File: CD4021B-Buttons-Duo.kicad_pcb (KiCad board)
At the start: 2 copper layers, 99.1 x 50.8 mm, 49 parts, among them J1 2.54, J10 JST XH, J11 JST XH, J12 JST XH, J13 JST XH, J14 JST XH, J15 JST XH, J16 JST XH, J17 JST XH, J2 JST XH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

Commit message: Cleanup via stitches
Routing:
- net GND: track 119.8 -> 111.2 mm, vias 49 -> 40
- net VCC: track 88.0 -> 93.0 mm
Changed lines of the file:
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@@
 (kicad_pcb (version 4) (host pcbnew 4.0.7)
   (general
-    (links 0)
-    (no_connects 2)
-    (area 105.334999 78.918999 204.545001 129.869001)
+    (links 153)
+    (no_connects 0)
+    (area 97.409048 78.918999 212.470953 129.869001)
     (thickness 1.6)
     (drawings 23)
-    (tracks 451)
+    (tracks 431)
     (zones 0)
     (modules 49)
@@
   (gr_line (start 204.47 78.994) (end 204.47 129.794) (layer Edge.Cuts) (width 0.15))
   (gr_line (start 105.41 78.994) (end 204.47 78.994) (layer Edge.Cuts) (width 0.15))
+  (segment (start 173.736 101.854) (end 175.26 101.854) (width 0.5) (layer F.Cu) (net 1) (status 30))
+  (segment (start 131.760454 101.838502) (end 133.284454 101.838502) (width 0.5) (layer F.Cu) (net 1) (status 30))
+  (segment (start 144.272 107.188) (end 142.24 107.188) (width 0.5) (layer B.Cu) (net 1) (status 30))
+  (segment (start 161.29 113.538) (end 161.29 122.428) (width 1) (layer B.Cu) (net 1))
+  (segment (start 154.94 107.188) (end 161.29 113.538) (width 1) (layer B.Cu) (net 1))
+  (segment (start 144.272 107.188) (end 154.94 107.188) (width 1) (layer B.Cu) (net 1) (status 10))
+  (via (at 161.29 122.428) (size 1.5) (drill 1.2) (layers F.Cu B.Cu) (net 1))
+  (segment (start 161.29 93.726) (end 161.29 86.614) (width 1) (layer F.Cu) (net 1))
   (segment (start 136.792 121.688) (end 139.192 121.688) (width 0.25) (layer F.Cu) (net 1) (status 30))
   (segment (start 136.792 86.36) (end 139.192 86.36) (width 0.25) (layer F.Cu) (net 1) (status 30))
   (segment (start 177.432 121.666) (end 179.832 121.666) (width 0.25) (layer F.Cu) (net 1) (status 30))
   (segment (start 177.432 86.338) (end 179.832 86.338) (width 0.25) (layer F.Cu) (net 1) (status 30))
-  (segment (start 144.272 107.188) (end 144.526 106.934) (width 1) (layer B.Cu) (net 1) (status 30))
-  (segment (start 144.526 106.934) (end 154.686 106.934) (width 1) (layer B.Cu) (net 1) (status 10))
-  (segment (start 154.686 106.934) (end 161.29 113.538) (width 1) (layer B.Cu) (net 1))
-  (segment (start 161.29 113.538) (end 161.29 119.126) (width 1) (layer B.Cu) (net 1))
-  (via (at 161.29 119.126) (size 1.5) (drill 1.2) (layers F.Cu B.Cu) (net 1))
   (segment (start 139.192008 105.917992) (end 139.192 105.918) (width 0.25) (layer F.Cu) (net 1))
   (segment (start 142.24 105.917992) (end 139.192008 105.917992) (width 0.25) (layer F.Cu) (net 1))
@@
   (segment (start 142.24 107.188) (end 142.24 105.917992) (width 0.25) (layer B.Cu) (net 1) (status 10))
   (via (at 142.24 105.917992) (size 0.6) (drill 0.4) (layers F.Cu B.Cu) (net 1))
-  (segment (start 142.24 107.188) (end 144.272 107.188) (width 1) (layer B.Cu) (net 1) (status 30))
   (segment (start 130.369956 101.854) (end 114.554 101.854) (width 1) (layer F.Cu) (net 1))
   (segment (start 173.736 101.854) (end 169.418 101.854) (width 1) (layer F.Cu) (net 1) (status 10))
   (segment (start 169.418 101.854) (end 161.29 93.726) (width 1) (layer F.Cu) (net 1))
-  (segment (start 161.29 93.726) (end 161.29 88.392) (width 1) (layer F.Cu) (net 1))
-  (segment (start 131.760454 101.838502) (end 133.104443 101.838502) (width 1) (layer F.Cu) (net 1) (status 30))
-  (segment (start 173.736 101.854) (end 175.26 101.854) (width 1) (layer F.Cu) (net 1) (status 30))
   (segment (start 131.760454 101.838502) (end 130.385454 101.838502) (width 1) (layer F.Cu) (net 1) (status 10))
   (segment (start 130.385454 101.838502) (end 130.369956 101.854) (width 1) (layer F.Cu) (net 1))
@@
   (via (at 167.64 102.616) (size 0.6) (drill 0.4) (layers F.Cu B.Cu) (net 2))
   (segment (start 152.654 105.156) (end 151.638 105.156) (width 0.25) (layer F.Cu) (net 2))
-  (via (at 151.638 105.156) (size 0.6) (drill 0.4) (layers F.Cu B.Cu) (net 2))
-  (segment (start 153.67 105.156) (end 152.654 105.156) (width 0.25) (layer B.Cu) (net 2))
-  (via (at 152.654 105.156) (size 0.6) (drill 0.4) (layers F.Cu B.Cu) (net 2))
-  (segment (start 154.686 105.156) (end 153.67 105.156) (width 0.25) (layer F.Cu) (net 2))
-  (via (at 153.67 105.156) (size 0.6) (drill 0.4) (layers F.Cu B.Cu) (net 2))
-  (segment (start 155.702006 105.156) (end 154.686 105.156) (width 0.25) (layer B.Cu) (net 2))
-  (via (at 154.686 105.156) (size 0.6) (drill 0.4) (layers F.Cu B.Cu) (net 2))
-  (segment (start 155.570006 105.288) (end 155.702006 105.156) (width 0.25) (layer B.Cu) (net 2))
-  (segment (start 155.702006 105.156006) (end 155.702006 105.156) (width 0.25) (layer B.Cu) (net 2))
-  (segment (start 156.464 105.918) (end 155.702006 105.156006) (width 0.25) (layer B.Cu) (net 2))
-  (via (at 155.702006 105.156) (size 0.6) (drill 0.4) (layers F.Cu B.Cu) (net 2))
-  (segment (start 157.226 106.68) (end 156.464 105.918) (width 0.25) (layer B.Cu) (net 2))
-  (via (at 156.464 105.918) (size 0.6) (drill 0.4) (layers F.Cu B.Cu) (net 2))
-  (segment (start 158.75 108.204) (end 159.512 108.966) (width 0.25) (layer F.Cu) (net 2))
-  (via (at 159.512 108.966) (size 0.6) (drill 0.4) (layers F.Cu B.Cu) (net 2))
-  (segment (start 157.988 107.442) (end 158.75 108.204) (width 0.25) (layer B.Cu) (net 2))
-  (via (at 158.75 108.204) (size 0.6) (drill 0.4) (layers F.Cu B.Cu) (net 2))
-  (segment (start 157.226 106.68) (end 157.988 107.442) (width 0.25) (layer F.Cu) (net 2))
-  (via (at 157.988 107.442) (size 0.6) (drill 0.4) (layers F.Cu B.Cu) (net 2))
-  (via (at 157.226 106.68) (size 0.6) (drill 0.4) (layers F.Cu B.Cu) (net 2))
+  (via (at 151.638 105.156) (size 0.6) (drill 0.4) (layers F.Cu B.Cu) (net 2) (status 1000000))
   (segment (start 110.236 109.474) (end 118.364 109.474) (width 1) (layer B.Cu) (net 2) (status 10))
   (segment (start 153.096 122.682) (end 154.94 122.682) (width 0.5) (layer B.Cu) (net 3) (status 30))

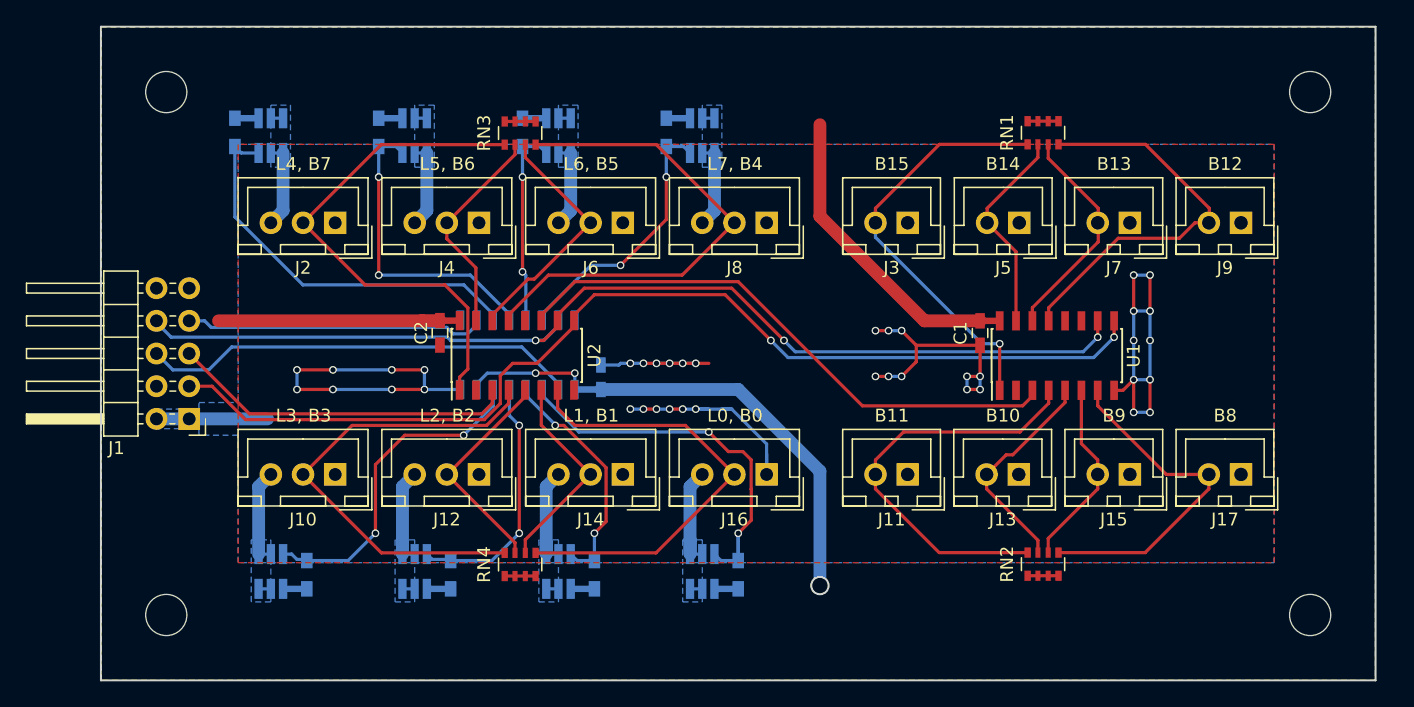
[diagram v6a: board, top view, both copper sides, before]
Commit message: Change the board dimension to be exactly 100x50mm
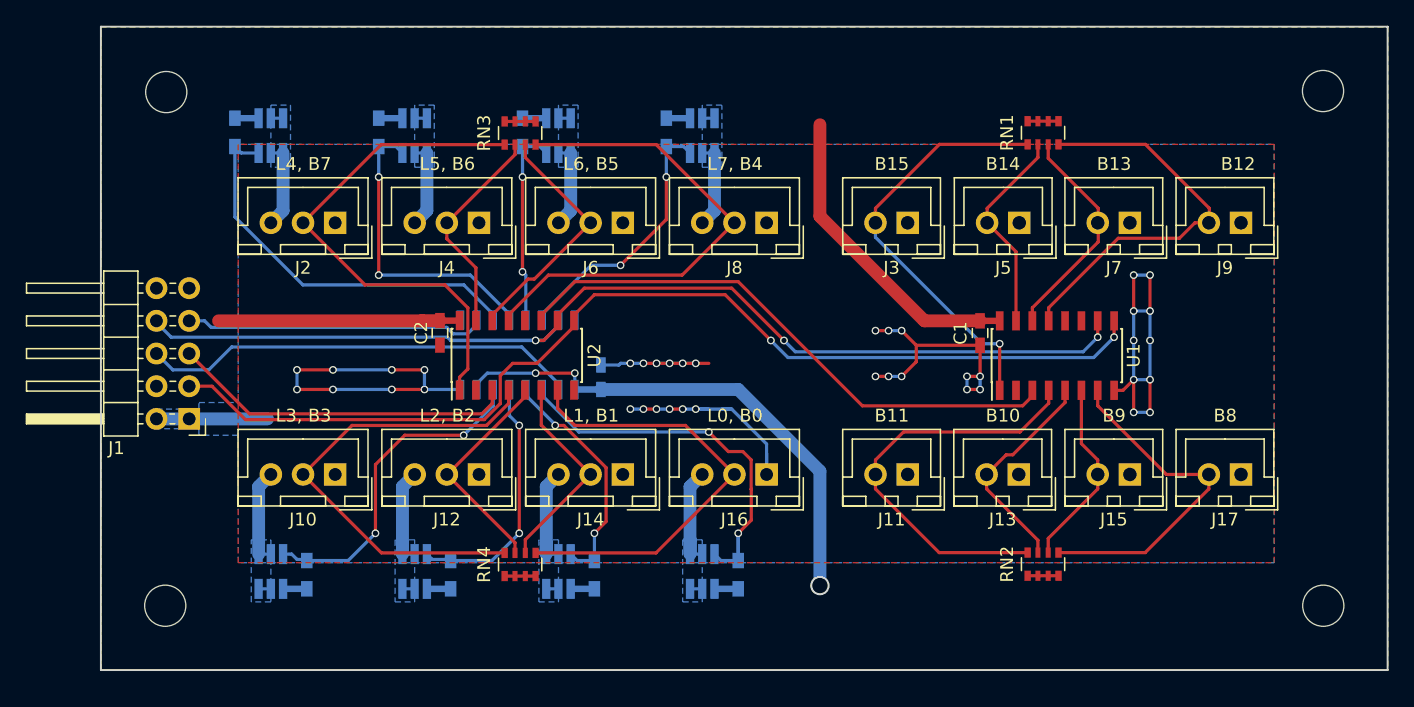
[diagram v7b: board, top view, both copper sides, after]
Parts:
- moved REF** 1.25 mm to (200.4, 124.0)
- moved REF** 1.00 mm to (200.4, 84.0)
- moved REF** 0.72 mm to (110.4, 124.0)
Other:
- board size 99.1 x 50.8 mm -> 100 x 50 mm
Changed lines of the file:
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@@
     (links 153)
     (no_connects 0)
-    (area 97.409048 78.918999 212.470953 129.869001)
+    (area 105.334999 78.918999 205.485001 129.069001)
     (thickness 1.6)
     (drawings 23)
@@
     (pad_to_mask_clearance 0)
     (aux_axis_origin 0 0)
+    (grid_origin 105.41 78.994)
     (visible_elements FFFFFF7F)
     (pcbplotparams
@@
   )
   (module Mounting_Holes:MountingHole_3.2mm_M3_ISO7380 (layer F.Cu)
-    (at 199.39 124.714)
+    (at 200.41 123.994)
     (descr "Mounting Hole 3.2mm, no annular, M3, ISO7380")
     (tags "mounting hole 3.2mm no annular m3 iso7380")
@@
   )
   (module Mounting_Holes:MountingHole_3.2mm_M3_ISO7380 (layer F.Cu)
-    (at 110.49 124.714)
+    (at 110.41 123.994)
     (descr "Mounting Hole 3.2mm, no annular, M3, ISO7380")
     (tags "mounting hole 3.2mm no annular m3 iso7380")
@@
   )
   (module Mounting_Holes:MountingHole_3.2mm_M3_ISO7380 (layer F.Cu)
-    (at 199.39 84.074)
+    (at 200.39 83.994)
     (descr "Mounting Hole 3.2mm, no annular, M3, ISO7380")
     (tags "mounting hole 3.2mm no annular m3 iso7380")
@@
     (effects (font (size 1 1) (thickness 0.15)))
   )
-  (gr_text B12 (at 192.786 89.662) (layer F.SilkS)
+  (gr_text B12 (at 193.786 89.662) (layer F.SilkS)
     (effects (font (size 1 1) (thickness 0.15)))
   )
@@
     (effects (font (size 1.5 1.5) (thickness 0.3)) (justify left mirror))
   )
-  (gr_line (start 105.41 129.794) (end 105.41 78.994) (layer Edge.Cuts) (width 0.15))
-  (gr_line (start 204.47 129.794) (end 105.41 129.794) (layer Edge.Cuts) (width 0.15))
-  (gr_line (start 204.47 78.994) (end 204.47 129.794) (layer Edge.Cuts) (width 0.15))
-  (gr_line (start 105.41 78.994) (end 204.47 78.994) (layer Edge.Cuts) (width 0.15))
+  (gr_line (start 105.41 128.994) (end 105.41 78.994) (layer Edge.Cuts) (width 0.15))
+  (gr_line (start 205.41 128.994) (end 105.41 128.994) (layer Edge.Cuts) (width 0.15))
+  (gr_line (start 205.41 78.994) (end 205.41 128.994) (layer Edge.Cuts) (width 0.15))
+  (gr_line (start 105.41 78.994) (end 205.41 78.994) (layer Edge.Cuts) (width 0.15))
   (segment (start 173.736 101.854) (end 175.26 101.854) (width 0.5) (layer F.Cu) (net 1) (status 30))
   (segment (start 131.760454 101.838502) (end 133.284454 101.838502) (width 0.5) (layer F.Cu) (net 1) (status 30))
@@
   (via (at 167.64 102.616) (size 0.6) (drill 0.4) (layers F.Cu B.Cu) (net 2))
   (segment (start 152.654 105.156) (end 151.638 105.156) (width 0.25) (layer F.Cu) (net 2))
-  (via (at 151.638 105.156) (size 0.6) (drill 0.4) (layers F.Cu B.Cu) (net 2) (status 1000000))
+  (via (at 151.638 105.156) (size 0.6) (drill 0.4) (layers F.Cu B.Cu) (net 2))
   (segment (start 110.236 109.474) (end 118.364 109.474) (width 1) (layer B.Cu) (net 2) (status 10))
   (segment (start 153.096 122.682) (end 154.94 122.682) (width 0.5) (layer B.Cu) (net 3) (status 30))
@@
     (polygon
       (pts
-        (xy 204.47 129.794) (xy 105.41 129.794) (xy 105.41 78.994) (xy 204.47 78.994)
+        (xy 205.41 128.994) (xy 105.41 128.994) (xy 105.41 78.994) (xy 205.41 78.994)
       )
     )
@@
     (polygon
       (pts
-        (xy 204.47 129.794) (xy 105.41 129.794) (xy 105.41 78.994) (xy 204.47 78.994)
+        (xy 205.41 128.994) (xy 105.41 128.994) (xy 105.41 78.994) (xy 205.41 78.994)
       )
     )
@@
     (polygon
       (pts
-        (xy 199.39 81.026) (xy 201.676 81.788) (xy 202.438 84.074) (xy 201.676 86.36) (xy 199.39 87.122)
-        (xy 197.104 86.36) (xy 196.342 84.074) (xy 197.104 81.788)
+        (xy 200.41 80.994) (xy 202.696 81.756) (xy 203.458 84.042) (xy 202.696 86.328) (xy 200.41 87.09)
+        (xy 198.124 86.328) (xy 197.362 84.042) (xy 198.124 81.756)
       )
     )
@@
     (polygon
       (pts
-        (xy 199.39 81.026) (xy 201.676 81.788) (xy 202.438 84.074) (xy 201.676 86.36) (xy 199.39 87.122)
-        (xy 197.104 86.36) (xy 196.342 84.074) (xy 197.104 81.788)
+        (xy 200.41 80.994) (xy 202.696 81.756) (xy 203.458 84.042) (xy 202.696 86.328) (xy 200.41 87.09)
+        (xy 198.124 86.328) (xy 197.362 84.042) (xy 198.124 81.756)
       )
     )
@@
     (polygon
       (pts
-        (xy 199.39 121.690263) (xy 201.676 122.452263) (xy 202.438 124.738263) (xy 201.676 127.024263) (xy 199.39 127.786263)
-        (xy 197.104 127.024263) (xy 196.342 124.738263) (xy 197.104 122.452263)
+        (xy 200.42422 120.994) (xy 202.71022 121.756) (xy 203.47222 124.042) (xy 202.71022 126.328) (xy 200.42422 127.09)
+        (xy 198.13822 126.328) (xy 197.37622 124.042) (xy 198.13822 121.756)
       )
     )
@@
     (polygon
       (pts
-        (xy 110.49 121.690263) (xy 112.776 122.452263) (xy 113.538 124.738263) (xy 112.776 127.024263) (xy 110.49 127.786263)
-        (xy 108.204 127.024263) (xy 107.442 124.738263) (xy 108.204 122.452263)
+        (xy 110.41 120.994) (xy 112.696 121.756) (xy 113.458 124.042) (xy 112.696 126.328) (xy 110.41 127.09)
+        (xy 108.124 126.328) (xy 107.362 124.042) (xy 108.124 121.756)
       )
     )
@@
     (polygon
       (pts
-        (xy 110.49 121.690263) (xy 112.776 122.452263) (xy 113.538 124.738263) (xy 112.776 127.024263) (xy 110.49 127.786263)
-        (xy 108.204 127.024263) (xy 107.442 124.738263) (xy 108.204 122.452263)
+        (xy 110.41 120.994) (xy 112.696 121.756) (xy 113.458 124.042) (xy 112.696 126.328) (xy 110.41 127.09)
+        (xy 108.124 126.328) (xy 107.362 124.042) (xy 108.124 121.756)
       )
     )
@@
     (polygon
       (pts
-        (xy 199.383276 121.686171) (xy 201.669276 122.448171) (xy 202.431276 124.734171) (xy 201.669276 127.020171) (xy 199.383276 127.782171)
-        (xy 197.097276 127.020171) (xy 196.335276 124.734171) (xy 197.097276 122.448171)
+        (xy 200.41 120.994) (xy 202.696 121.756) (xy 203.458 124.042) (xy 202.696 126.328) (xy 200.41 127.09)
+        (xy 198.124 126.328) (xy 197.362 124.042) (xy 198.124 121.756)
       )
     )

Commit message: Move logo (again)
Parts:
- moved REF*** 4.31 mm to (169.6, 121.0)
- moved REF*** 3.97 mm to (181.6, 121.0)
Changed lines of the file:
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@@
   )
   (module Symbols:OSHW-Logo2_7.3x6mm_SilkScreen (layer B.Cu)
-    (at 170.434 125.222 180)
+    (at 169.61 120.994 180)
     (descr "Open Source Hardware Symbol")
     (tags "Logo Symbol OSHW")
@@
   )
   (module Symbols:KiCad-Logo2_6mm_SilkScreen (layer B.Cu)
-    (at 181.61 124.968 180)
+    (at 181.61 120.994 180)
     (descr "KiCad Logo")
     (tags "Logo KiCad")
